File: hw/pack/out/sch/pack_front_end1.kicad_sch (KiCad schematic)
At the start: 17 parts, among them J1 3.5mm locking, U3 OPA1656

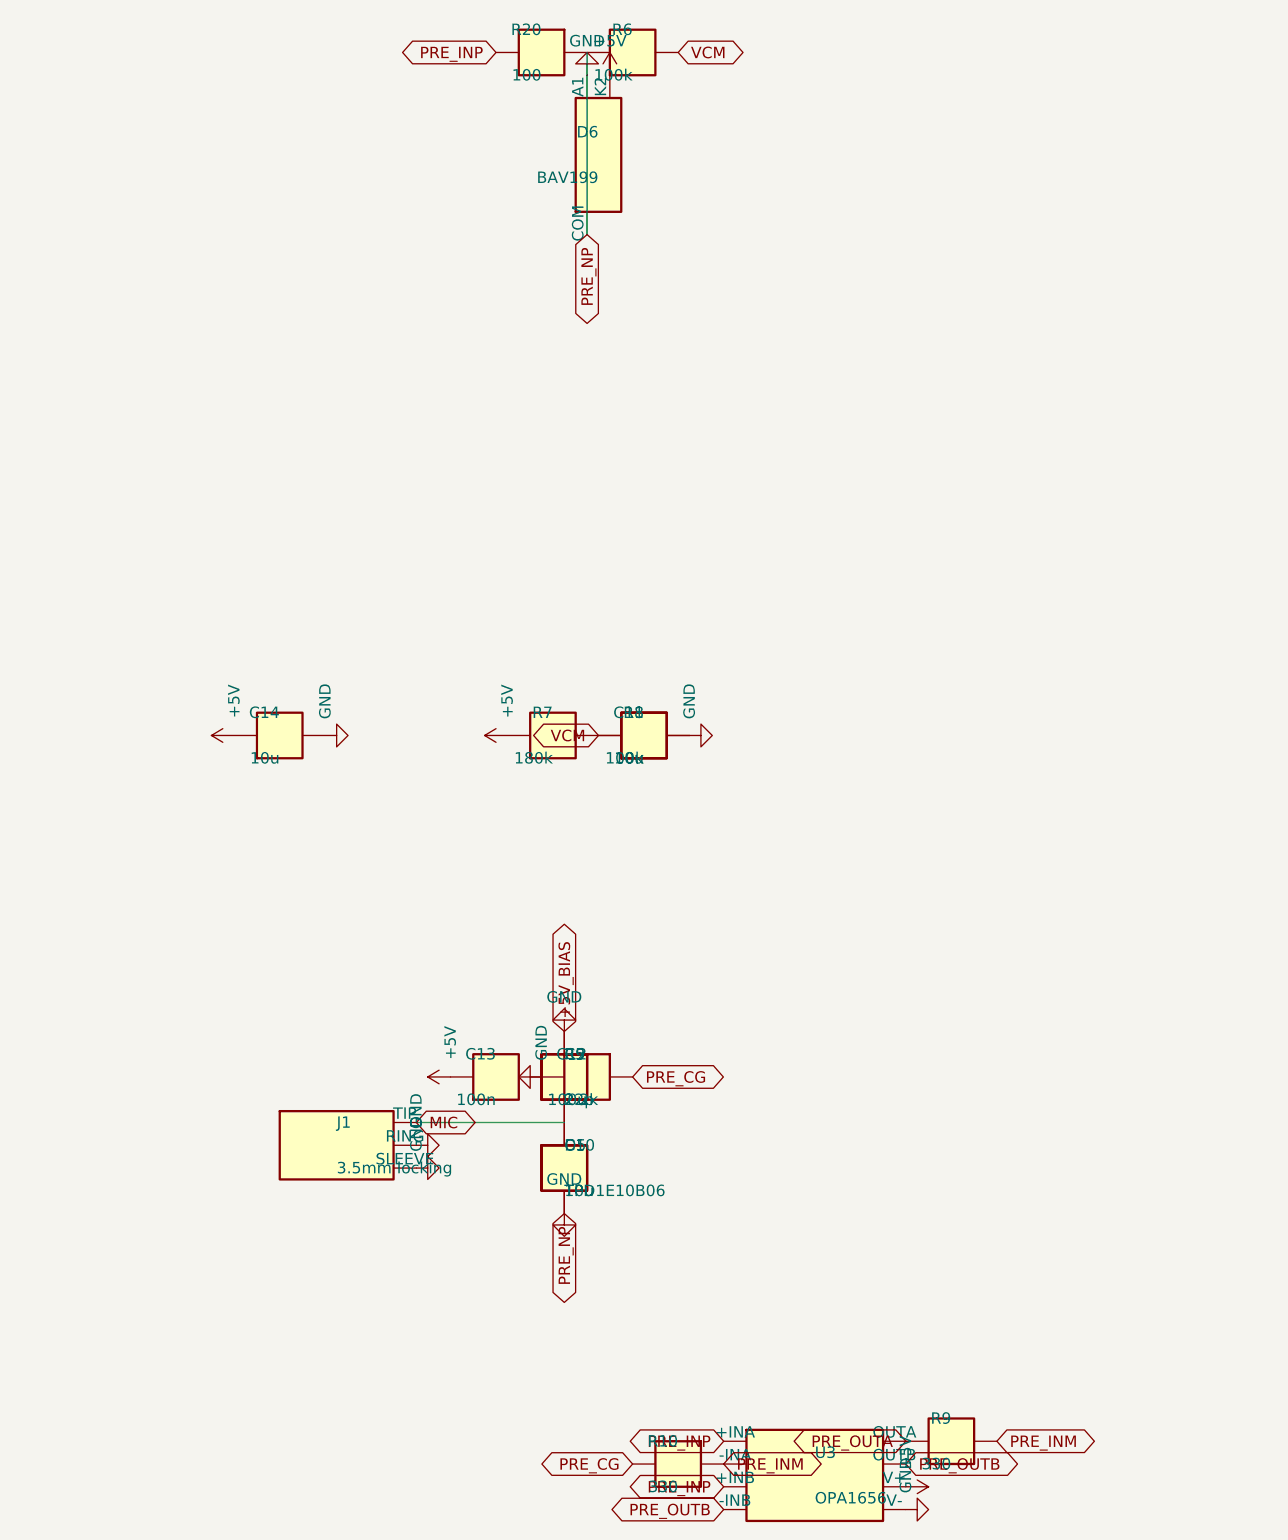
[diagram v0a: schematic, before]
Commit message: hw/pack: 4-layer pack PCB layout, review fixes, fab outputs, cost-down (#104)
* hw/pack: scripted 4-layer layout from the netlist, DRC clean (#34)

layout.py builds pack.kicad_pcb from out/pack.net with pcbnew: outline from
mech/pack.py, BT40NE antenna past the board edge, TI-pattern boost cell,
grid maze router (router.py), GND fan-out vias, RF via fence, JLC rules in
pack.kicad_dru. outputs.py writes gerbers/drill/BOM/CPL/STEP and renders.

Co-Authored-By: Claude Opus 5.5 <noreply@anthropic.com>

* hw/pack: enclosure fit (fit.py + CadQuery test), mech outline from the layout, layout tests (#34)

mech/pack.py takes the real outline (73.4 x 35 mm, post notch), z0 +1.4 mm so
the module antenna clears the clip bosses, and the antenna overhang as a part.
fit.py checks board/parts/openings/lid features without CadQuery and renders
fit_top/fit_side.png; tests/mech/test_pack_fit.py does it with the STEP.
tests/test_pack_layout.py: DRC 0 errors, fab outputs fresh, netlist parity.

Co-Authored-By: Claude Opus 5.5 <noreply@anthropic.com>

* hw/REVIEW.md: pack board layout review, fixes and open items (#34)

Co-Authored-By: Claude Opus 5.5 <noreply@anthropic.com>

* hw/pack, mech: SJ1-3543 from datasheet, M2 board retention, light pipes, switch fork, CI pcb job (#34)

- SJ1-3543 footprint from Same Sky SJ1-354X (09/2024): 12x11.6x9.6 body, M6
  bushing through the wall from the inner face, axis 5.2 mm, anchors on GND
- H1/H2 M2 holes + printed pilot bosses (mech PCB_SCREWS), two rests
- lid light-pipe chimneys (lid prints outer-face-down), printed switch fork
  straddling SW1's right-angle actuator through a relocated slot
- mech comps() now the per-part envelope from the layout
- fit.py checks fork, chimneys, screws; CadQuery fit test mandatory under CI
- ci.yml: pcb job (KiCad 10 PPA) runs tests/test_pack_layout.py
- REVIEW: holder BH-18650-W and pigtail Molex 0731160017 chosen; with them
  PK-12 would be ~$38.2 > $35, prices.py left unchanged pending decision

Co-Authored-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
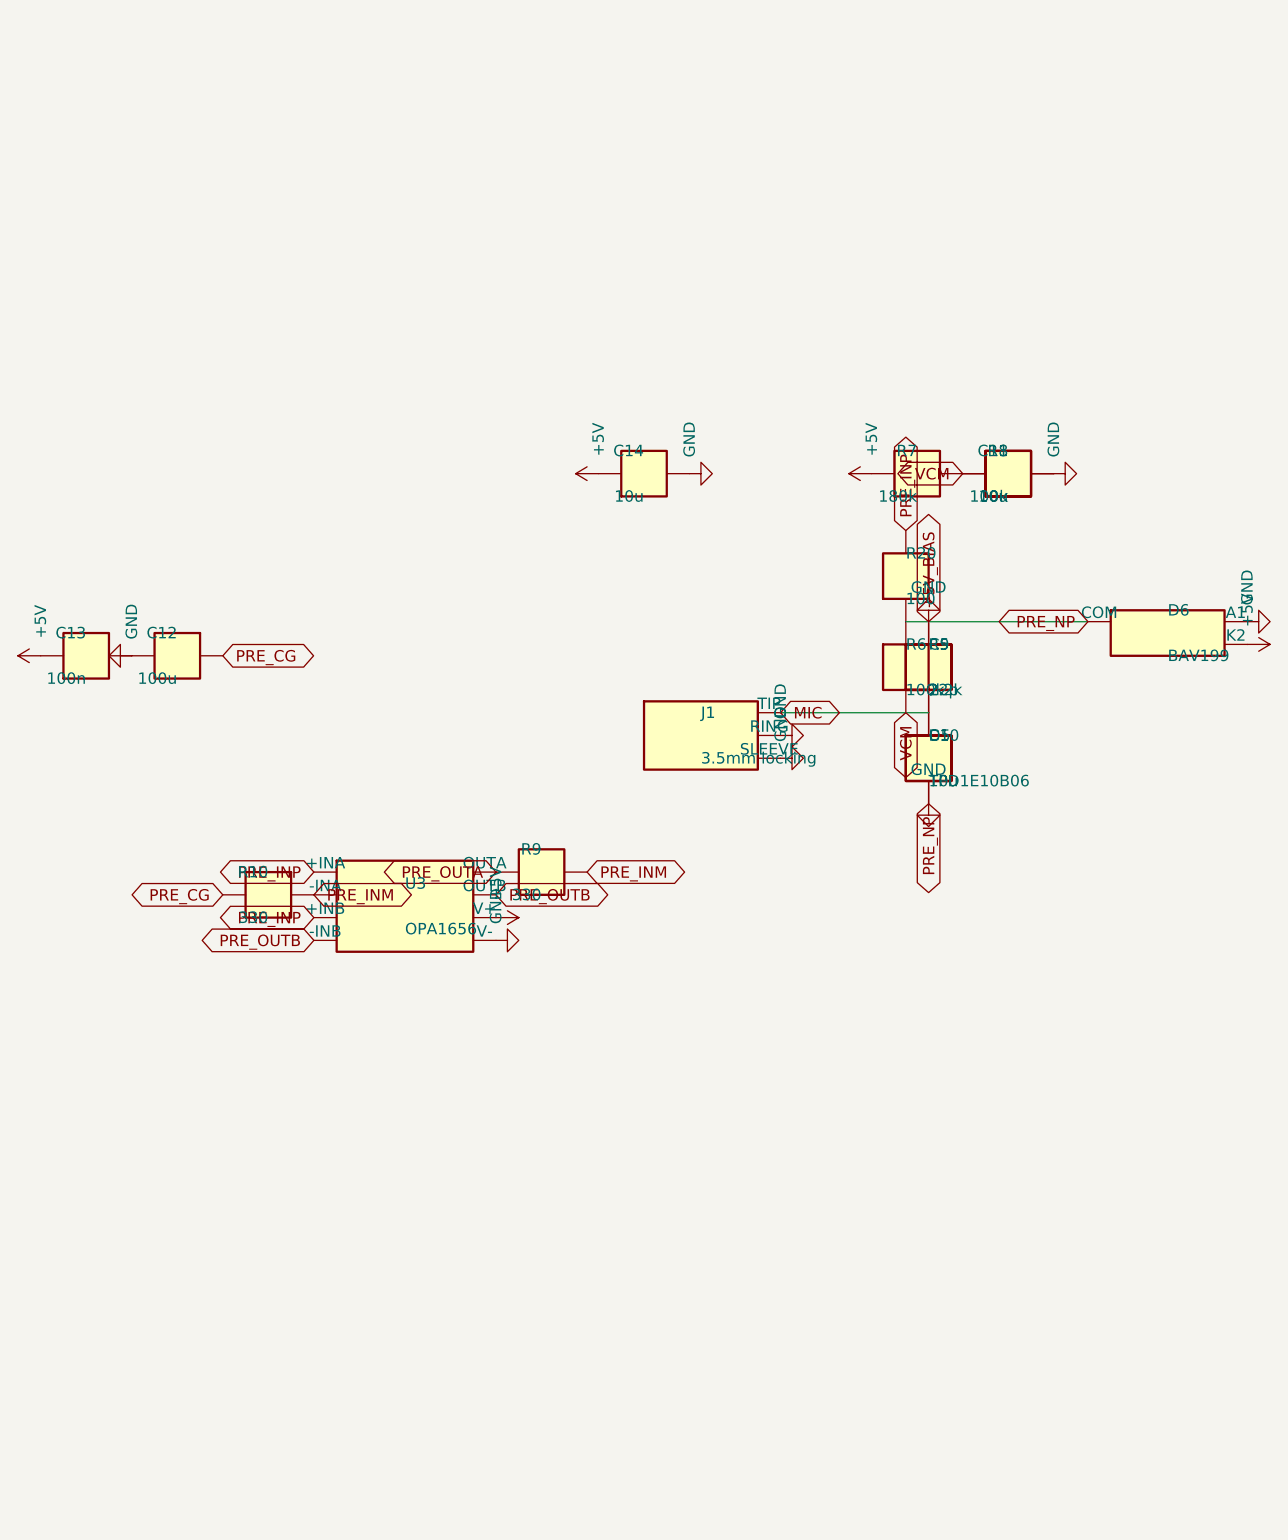
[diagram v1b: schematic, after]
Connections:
- net VCM is gone; now on net MIC: C11.1, R6.2, R7.2, R8.1
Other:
- moved on the sheet: C10, C11, C12, C13, C14, C9, D5, D6, J1, R10, R20, R5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
